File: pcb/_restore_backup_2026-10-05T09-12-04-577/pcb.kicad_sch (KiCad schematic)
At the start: 7 parts, among them SW4 SW_Push, SW5 SW_Push, SW6 SW_Push, U1 RP2040

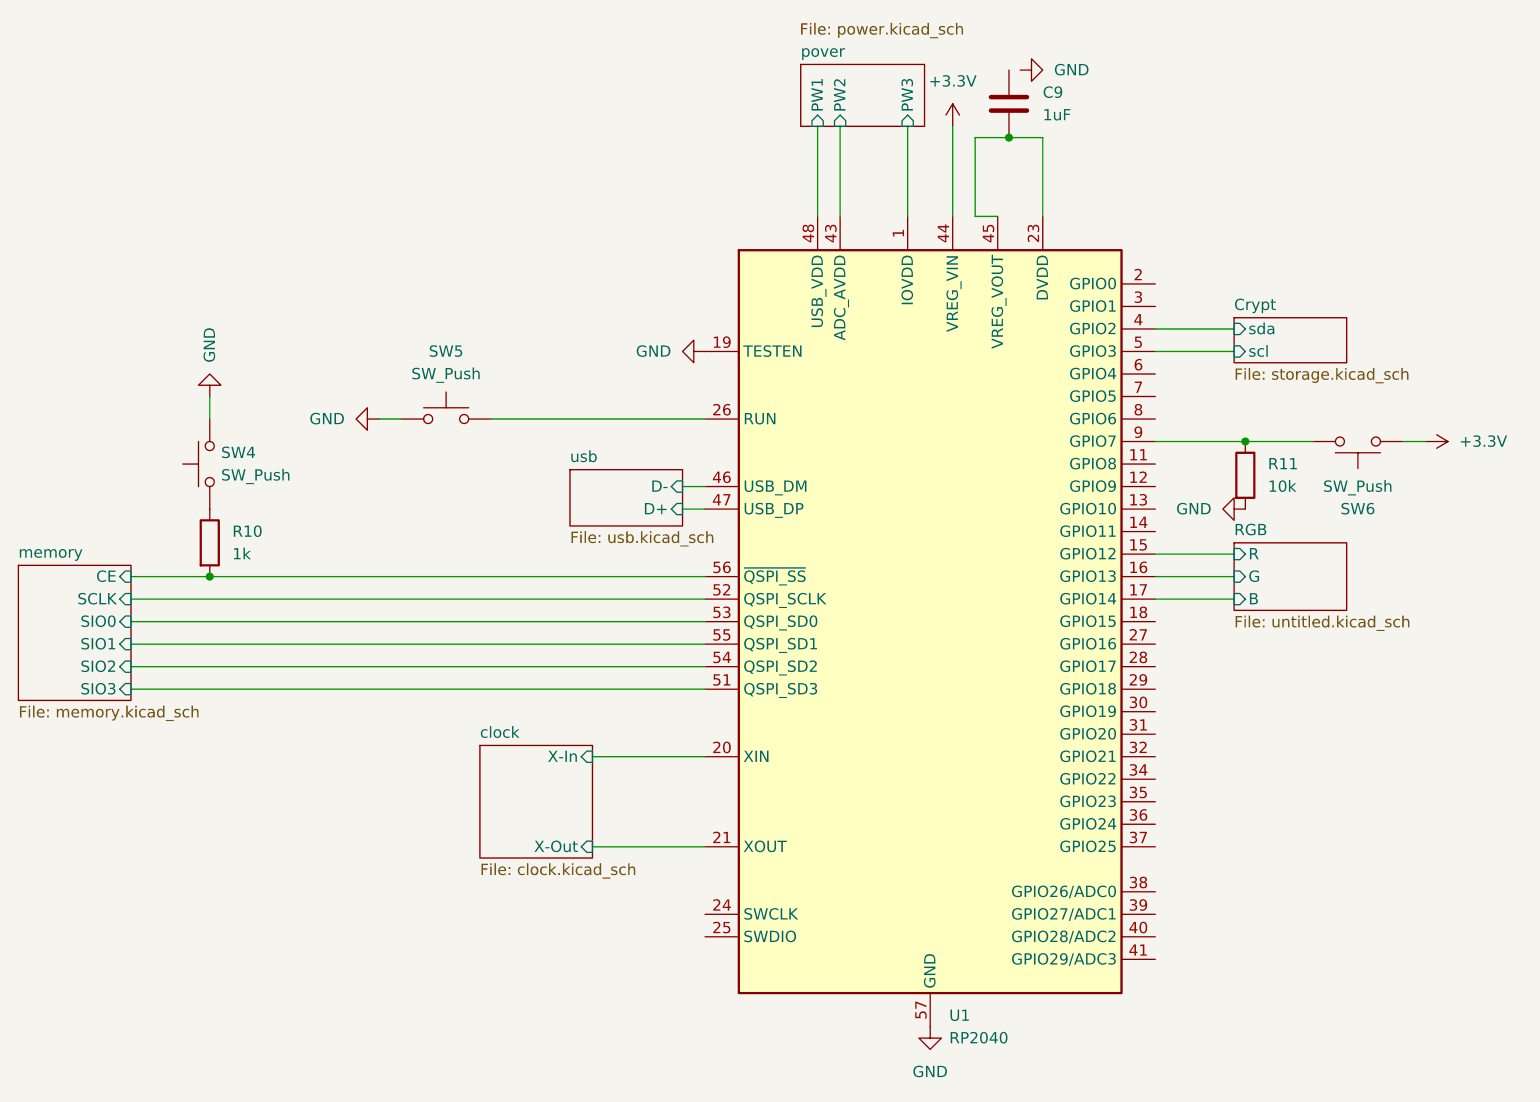
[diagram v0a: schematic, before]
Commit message: making the power delivery
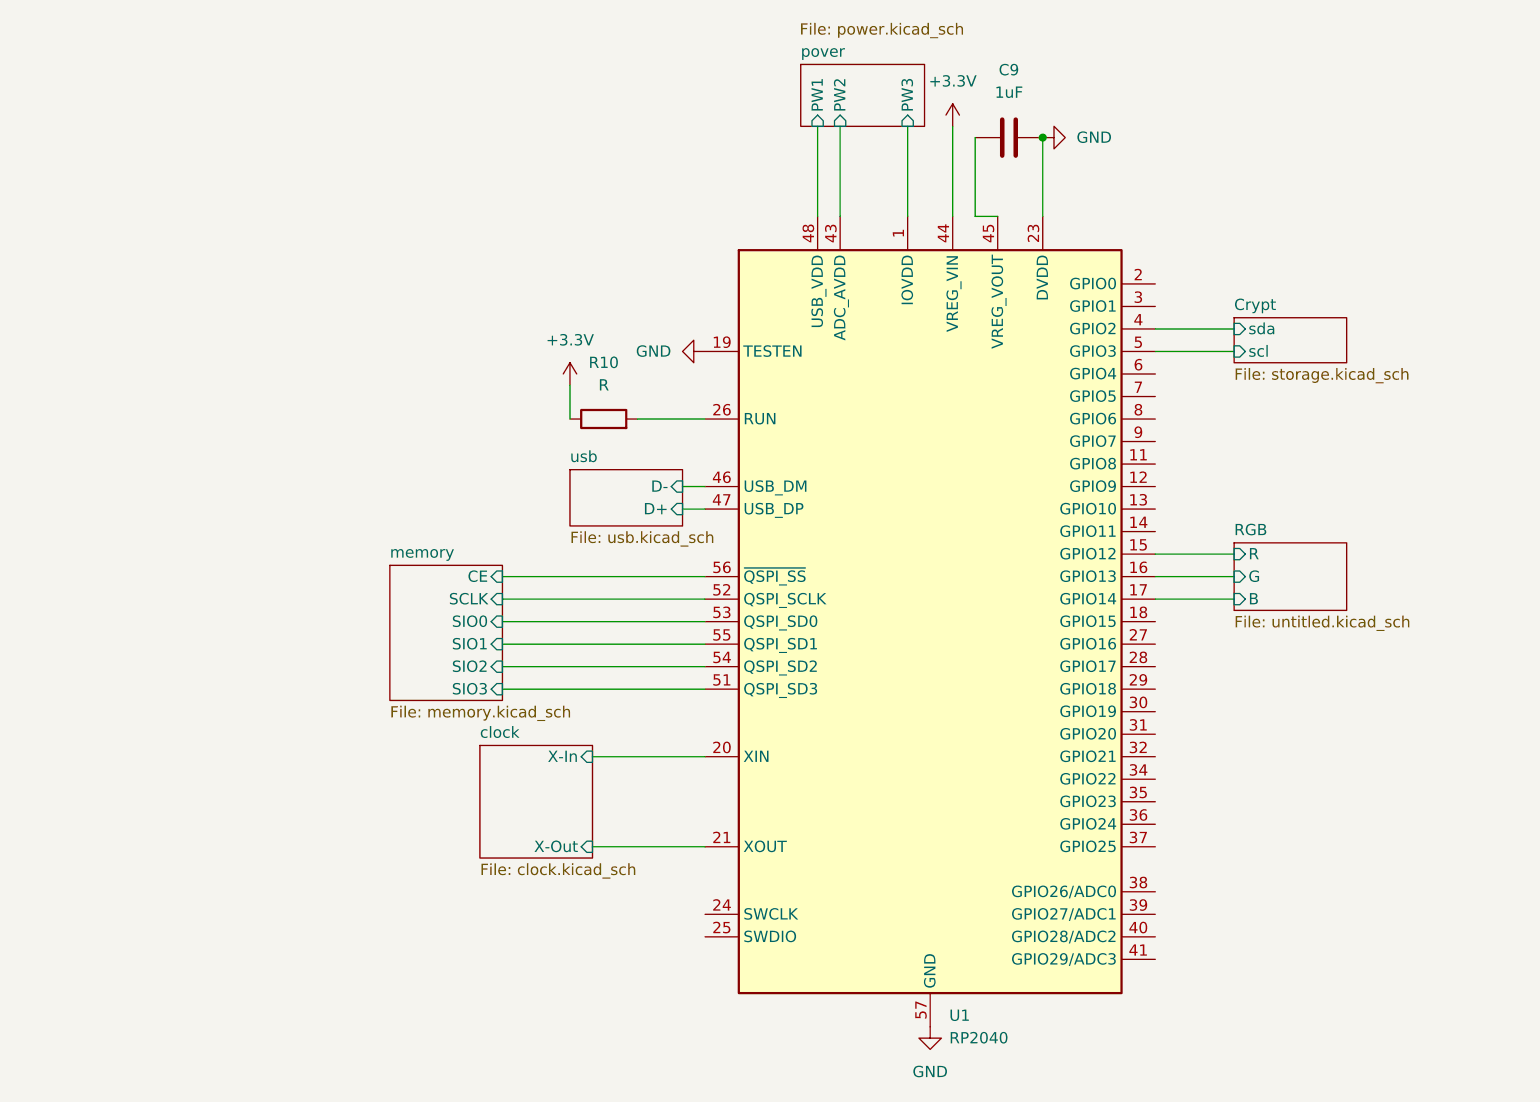
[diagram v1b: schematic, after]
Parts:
- removed R11: 10k, symbol Device:R
- removed SW4, SW5, SW6: SW_Push, Package_TO_SOT_SMD:SOT-23-6, symbol Switch:SW_Push
- R10: value 1k -> R
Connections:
- net +3.3V: now also R10.1
- net GND: now also C9.2, U1.23 (DVDD), U1.50 (DVDD)
- net memory/CE: no longer R10.2
- net at U1.26 (RUN): now also R10.2
- net at C9.1, U1.45 (VREG_VOUT): no longer U1.23 (DVDD), U1.50 (DVDD)
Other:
- moved on the sheet: C9
